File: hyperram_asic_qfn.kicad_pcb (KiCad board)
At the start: 4 copper layers, 59.5 x 60 mm, 45 parts, among them IC1 W25Q32JVSSIQ_TR, IC2 S27KL0641DABHI020, IC3 LP5907UVX-1.8_NOPB, IC4 LP5907UVX-3.3_NOPB, IC5 LP5907MFX-3.3_NOPB, IC6 MCP1824T-1802E_OT, J1 USB_B_Micro, J2 Conn_02x03_Counter_Clockwise, J3 1156915, J4 1156915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

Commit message: First try on component placement and routing.
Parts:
- added C19: 100n, Capacitor_SMD:C_0402_1005Metric_Pad0.74x0.62mm_HandSolder, F.Cu at (115.3, 70.6)
- added C20: 100n, Capacitor_SMD:C_0402_1005Metric_Pad0.74x0.62mm_HandSolder, F.Cu at (115.3, 72.6)
- added C21: 100n, Capacitor_SMD:C_0402_1005Metric_Pad0.74x0.62mm_HandSolder, F.Cu at (115.3, 74.5)
- added C22: 22u 25v, Capacitor_SMD:C_0805_2012Metric_Pad1.18x1.45mm_HandSolder, F.Cu at (111.3, 71.1)
- added C23: 1u 16v, Capacitor_SMD:C_0805_2012Metric_Pad1.18x1.45mm_HandSolder, F.Cu at (111.3, 74.1)
- added C24: 22u 25v, Capacitor_SMD:C_0805_2012Metric_Pad1.18x1.45mm_HandSolder, F.Cu at (111.3, 77.1)
- added J7: Conn_02x10_Odd_Even, Connector_PinHeader_2.54mm:PinHeader_2x10_P2.54mm_Vertical, F.Cu at (171.3, 73.0)
- added R5: 0, Resistor_SMD:R_0603_1608Metric, F.Cu at (176.5, 90.3)
- added R6: NC, Resistor_SMD:R_0603_1608Metric, F.Cu at (176.6, 87.6)
- added TP7: TestPoint, TestPoint:TestPoint_Pad_D1.0mm, F.Cu at (175.7, 93.2)
- C10, C2, C4, C5, C6, C7, C8, C9: value 22n -> 100n
- C18: value 1u 16v -> 100n; footprint Capacitor_SMD:C_0805_2012Metric_Pad1.18x1.45mm_HandSolder -> Capacitor_SMD:C_0402_1005Metric_Pad0.74x0.62mm_HandSolder
- J2: value Conn_02x03_Counter_Clockwise -> Conn_02x06_Odd_Even; footprint Connector_PinHeader_2.54mm:PinHeader_2x03_P2.54mm_Vertical -> Connector_PinHeader_2.54mm:PinHeader_2x06_P2.54mm_Vertical
- R4: value 220 -> 2k2
- U1: value CARAVEL -> CARAVEL_QFN; footprint hyperram_asic_qfn:WLCSP-60_P0.5mm -> Package_DFN_QFN:QFN-64-1EP_9x9mm_P0.5mm_EP7.65x7.65mm
- moved D2 71.1 mm to (101.6, 71.9)
- moved R2 71.1 mm to (101.6, 77.2)
- moved J2 54.7 mm to (126.0, 92.3), turned to 0 degrees
- moved C1 53.6 mm to (112.8, 96.9)
- moved IC1 53.6 mm to (117.4, 99.9)
- moved R3 39.4 mm to (147.2, 105.7)
- moved J4 39.4 mm to (148.5, 114.8), turned to 180 degrees
- moved RN3 28.2 mm to (182.0, 105.8)
- moved RN1 27.8 mm to (153.6, 105.7)
- moved J3 24.7 mm to (179.5, 114.8), turned to 180 degrees
- moved TP2 20.1 mm to (136.8, 85.5), turned to -90 degrees
- moved TP5 17.6 mm to (143.4, 85.5), turned to -90 degrees
- moved Y1 17.2 mm to (135.7, 79.3), turned to -90 degrees
- moved C6 17.0 mm to (144.1, 91.0)
- moved C10 16.7 mm to (144.4, 95.1)
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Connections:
- C10 pad 1: +1V8 -> VCC
- C17 pad 1: +1V8 -> VCC
- C6 pad 1: +1V8 -> VCC
- C8 pad 1: +1V8 -> VCC
- J2 pad 1: /mgmt_spi_cs -> +3V3
- J2 pad 2: /mgmt_spi_di -> +3V3
- J2 pad 3: /mgmt_spi_clk -> GND
- J2 pad 6: +5V -> /mgmt_spi_di
- RN1 pad 1: /cvl_hr_csn -> /cvl_hr_rwds
- RN1 pad 2: /cvl_hr_clk -> /cvl_hr_clkn
- RN1 pad 3: /cvl_hr_clkn -> /cvl_hr_clk
- RN1 pad 4: /cvl_hr_rwds -> /cvl_hr_csn
- RN1 pad 5: /hr_rwds -> /hr_csn
- RN1 pad 6: /hr_clkn -> /hr_clk
- RN1 pad 7: /hr_clk -> /hr_clkn
- RN1 pad 8: /hr_csn -> /hr_rwds
- RN2 pad 1: /cvl_hr_dq0 -> /cvl_hr_dq3
- RN2 pad 2: /cvl_hr_dq1 -> /cvl_hr_dq2
- RN2 pad 3: /cvl_hr_dq2 -> /cvl_hr_dq1
- RN2 pad 4: /cvl_hr_dq3 -> /cvl_hr_dq0
- RN2 pad 5: /hr_dq3 -> /hr_dq0
- RN2 pad 6: /hr_dq2 -> /hr_dq1
- RN2 pad 7: /hr_dq1 -> /hr_dq2
- RN2 pad 8: /hr_dq0 -> /hr_dq3
- RN3 pad 1: /cvl_hr_dq4 -> /cvl_hr_dq7
- RN3 pad 2: /cvl_hr_dq5 -> /cvl_hr_dq6
- RN3 pad 3: /cvl_hr_dq6 -> /cvl_hr_dq5
- RN3 pad 4: /cvl_hr_dq7 -> /cvl_hr_dq4
- RN3 pad 5: /hr_dq7 -> /hr_dq4
- RN3 pad 6: /hr_dq6 -> /hr_dq5
- RN3 pad 7: /hr_dq5 -> /hr_dq6
- RN3 pad 8: /hr_dq4 -> /hr_dq7
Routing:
- net GND: track 132.3 -> 40.9 mm, vias 80 -> 35
- net /hr_rstn: track 35.9 -> 5.40 mm
- net /mgmt_spi_do: track 30.4 -> 0.00 mm
- net +3V3: track 55.4 -> 26.1 mm, vias 14 -> 9
- net /hr_dq2: track 26.8 -> 0.00 mm, vias 2 -> 0
- net /hr_csn: track 33.7 -> 7.68 mm
- net /hr_dq3: track 28.6 -> 3.61 mm
- net /cvl_hr_rstn: track 22.7 -> 0.00 mm
- net /hr_dq1: track 22.7 -> 0.00 mm
- net /hr_clk: track 31.0 -> 10.1 mm
- net /flash_clk: track 20.1 -> 0.00 mm
- net +1V8: track 24.2 -> 4.55 mm, vias 7 -> 0
- net /mgmt_spi_di: track 19.4 -> 0.00 mm
- net /cvl_hr_csn: track 19.0 -> 0.00 mm
- net /mgmt_spi_clk: track 18.7 -> 0.00 mm
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- removed copper zone on B.Cu, net +1V8
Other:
- board size 59.5 x 60 mm -> 79.5 x 70 mm

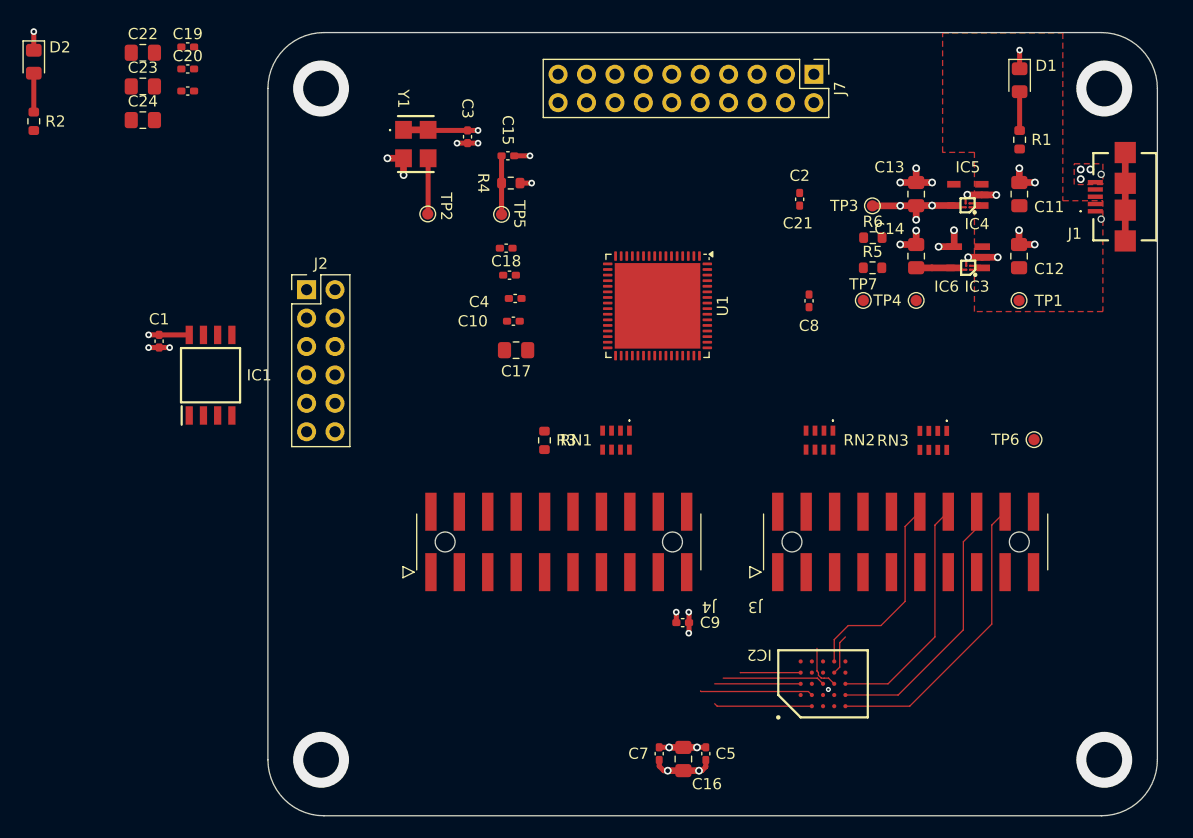
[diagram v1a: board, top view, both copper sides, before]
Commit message: Adjusted placement of some components and started routing tracks between ASIC and HyperRAM chip.
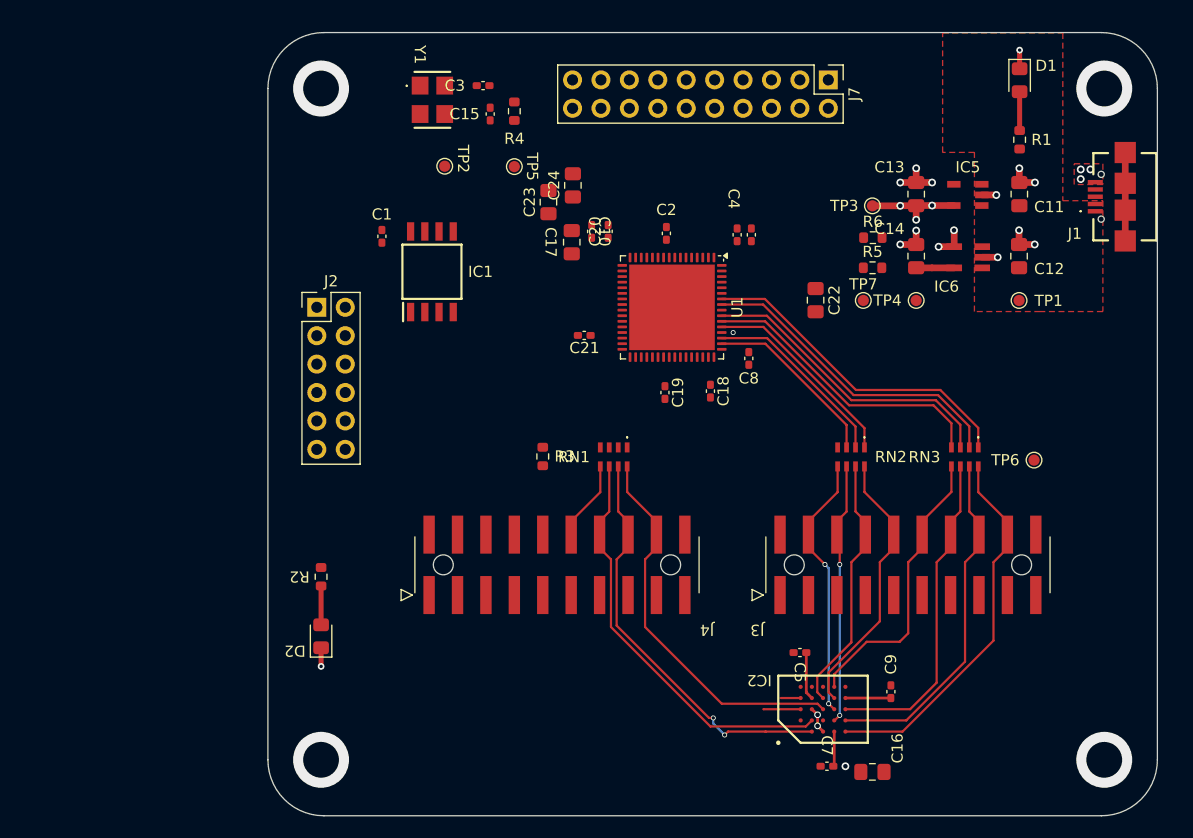
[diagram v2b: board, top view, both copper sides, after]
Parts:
- removed IC3: LP5907UVX-1.8_NOPB, hyperram_asic_qfn:BGA4C35P2X2_64X64X44
- removed IC4: LP5907UVX-3.3_NOPB, hyperram_asic_qfn:BGA4C35P2X2_64X64X33
- moved C22 64.1 mm to (171.4, 93.2), turned to -90 degrees
- moved D2 57.4 mm to (127.3, 123.3), turned to 90 degrees
- moved C19 52.7 mm to (158.0, 101.5), turned to -90 degrees
- moved R2 48.1 mm to (127.3, 117.9), turned to -90 degrees
- moved C21 41.6 mm to (150.8, 96.4), turned to 180 degrees
- moved C20 40.3 mm to (152.9, 87.1), turned to 90 degrees
- moved C24 38.9 mm to (149.8, 83.0), turned to 90 degrees
- moved C23 37.7 mm to (147.6, 84.5), turned to 90 degrees
- moved C18 22.3 mm to (162.1, 101.3), turned to -90 degrees
- moved C1 22.0 mm to (132.7, 87.5)
- moved C6 21.9 mm to (165.7, 87.4), turned to 90 degrees
- moved IC1 21.8 mm to (137.2, 90.7)
- moved C4 20.6 mm to (164.4, 87.4), turned to 90 degrees
- moved C9 19.6 mm to (178.2, 128.2), turned to 90 degrees
- moved C16 16.9 mm to (176.5, 135.4), turned to 0 degrees
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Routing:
- net /cvl_hr_dq7: track 0.00 -> 29.4 mm
- net /cvl_hr_dq6: track 0.00 -> 28.5 mm
- net /hr_clkn: track 8.78 -> 36.9 mm, vias 0 -> 2
- net /cvl_hr_dq5: track 0.00 -> 27.4 mm
- net /hr_clk: track 10.1 -> 37.0 mm
- net /cvl_hr_dq4: track 0.00 -> 26.5 mm
- net /hr_rwds: track 9.13 -> 34.8 mm
- net /hr_dq1: track 0.00 -> 23.4 mm, vias 0 -> 2
- net /hr_dq2: track 0.00 -> 23.1 mm
- net /hr_dq3: track 3.61 -> 24.4 mm
- net /hr_dq0: track 4.19 -> 23.7 mm, vias 0 -> 2
- net /cvl_hr_dq3: track 0.00 -> 18.2 mm
- net GND: track 40.9 -> 23.4 mm, vias 35 -> 25
- net /cvl_hr_dq2: track 0.00 -> 17.1 mm
- net /cvl_hr_dq1: track 0.00 -> 16.2 mm
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
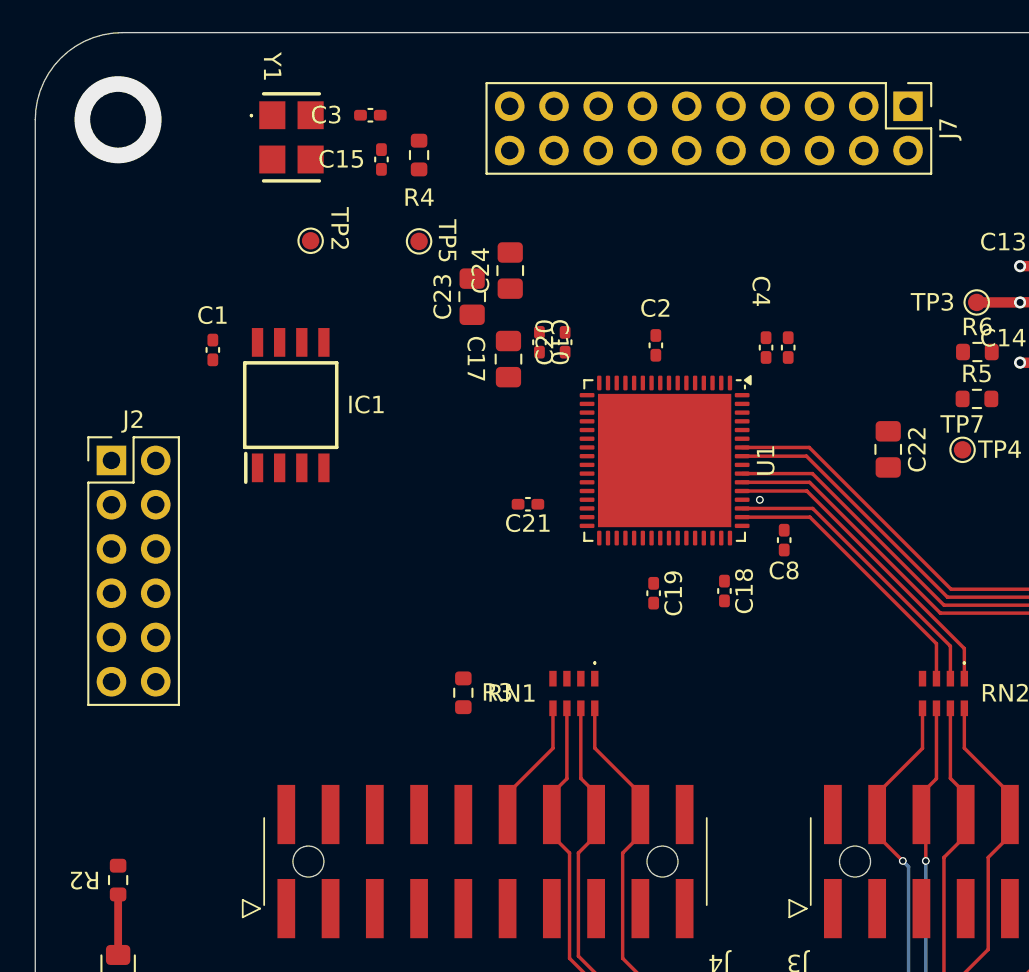
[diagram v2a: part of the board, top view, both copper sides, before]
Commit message: First try for routing digital signals (DSPI, GPIOs, CLK, RST)
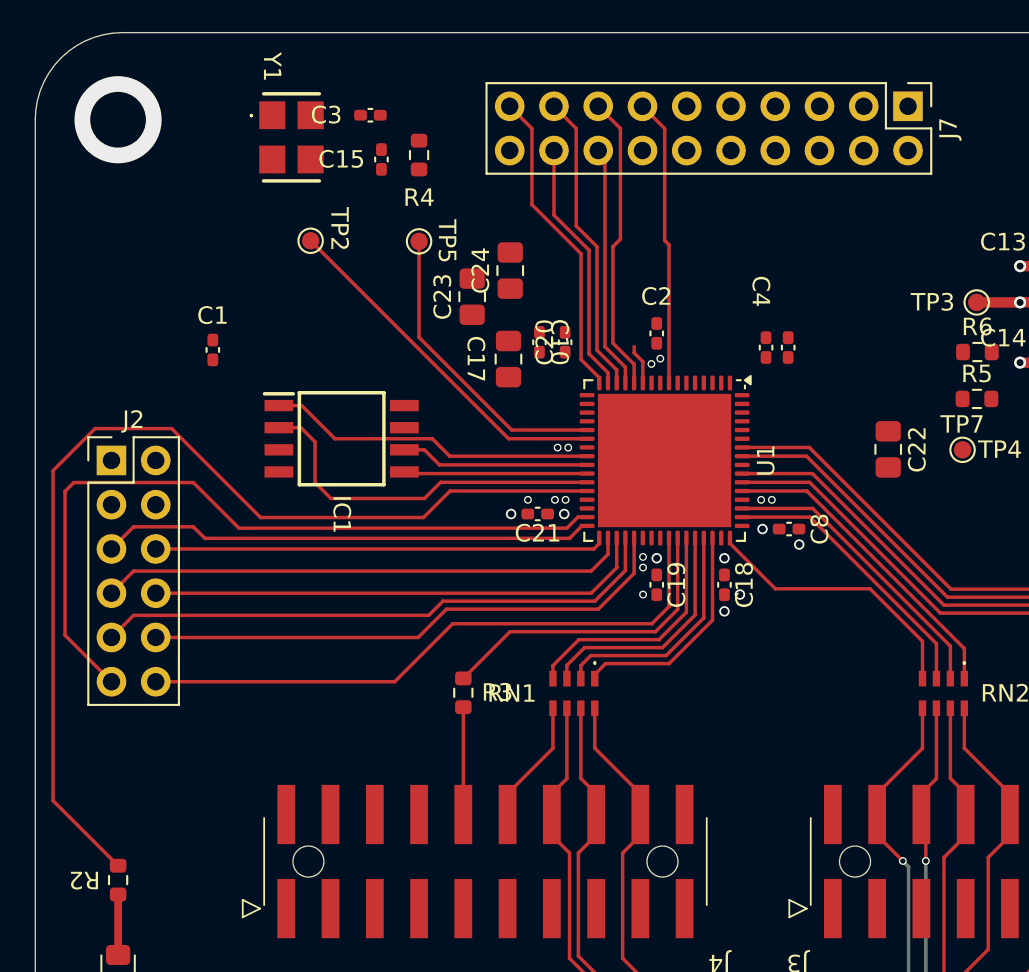
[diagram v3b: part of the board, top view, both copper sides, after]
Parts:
- moved IC1 3.50 mm to (140.1, 92.6), turned to 0 degrees
- moved C21 0.79 mm to (151.3, 96.9)
- moved C8 0.69 mm to (165.8, 97.8), turned to 0 degrees
- moved C2 0.69 mm to (158.2, 86.6)
- moved C19 0.51 mm to (158.2, 101.0)
- moved C18 0.36 mm to (162.1, 101.0)
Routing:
- net /gpio: track 0.00 -> 58.6 mm
- net /gpio0: track 0.00 -> 43.5 mm
- net /gpio7: track 0.00 -> 35.2 mm
- net /uart_rx: track 0.00 -> 32.9 mm
- net /uart_tx: track 0.00 -> 31.0 mm
- net /mgmt_spi_cs: track 0.00 -> 30.4 mm
- net /mgmt_spi_clk: track 0.00 -> 28.8 mm
- net /mgmt_spi_do: track 0.00 -> 28.4 mm
- net /mgmt_spi_di: track 0.00 -> 25.9 mm
- net /flash_io1: track 0.00 -> 21.1 mm
- net /clock: track 0.00 -> 20.6 mm
- net /flash_csb: track 0.00 -> 18.9 mm
- net /cvl_hr_rstn: track 0.00 -> 18.0 mm
- net /gpio37: track 0.00 -> 18.0 mm
- net /gpio35: track 0.00 -> 17.4 mm
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
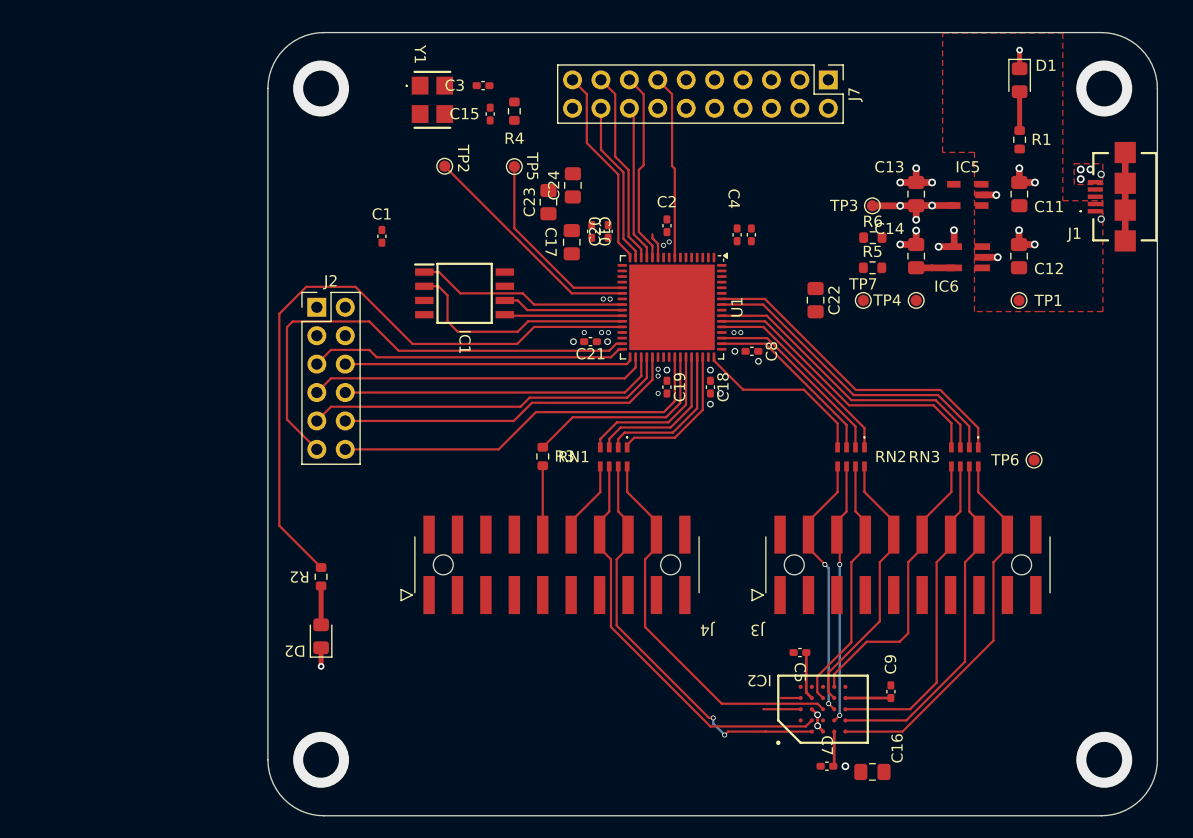
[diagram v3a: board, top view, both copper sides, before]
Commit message: Improved placement. Routed all digital signals.
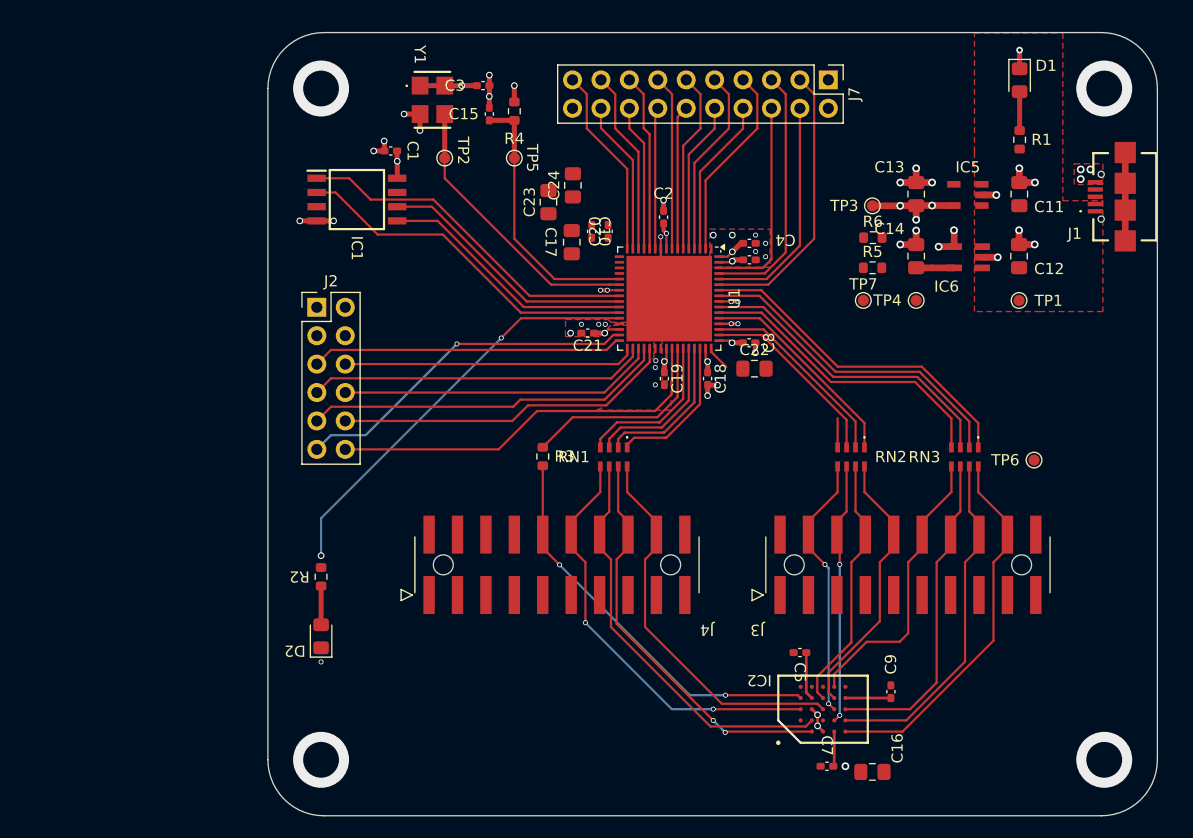
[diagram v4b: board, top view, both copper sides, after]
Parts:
- moved IC1 12.8 mm to (130.5, 84.2)
- moved C22 8.20 mm to (166.0, 99.3), turned to 0 degrees
- moved C1 7.67 mm to (133.5, 79.9), turned to 180 degrees
- moved C6 2.24 mm to (165.5, 89.6), turned to 0 degrees
- moved C4 1.33 mm to (165.5, 88.1), turned to 0 degrees
- moved C2 0.82 mm to (157.9, 85.8)
- moved U1 0.82 mm to (158.4, 93.1)
- moved C21 0.80 mm to (151.1, 96.2)
- moved C18 0.80 mm to (161.8, 100.2)
- moved C8 0.80 mm to (165.5, 97.0)
- moved C19 0.80 mm to (157.9, 100.2)
- moved TP5 0.76 mm to (144.5, 80.5)
- moved TP2 0.73 mm to (138.3, 80.5)
- moved C15 0.08 mm to (142.3, 76.6)
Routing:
- net /hr_rstn: track 7.93 -> 36.0 mm, vias 0 -> 2
- net /hr_csn: track 10.5 -> 38.0 mm, vias 0 -> 2
- net /gpio21: track 0.00 -> 24.9 mm
- net GND: track 23.4 -> 47.1 mm, vias 39 -> 56
- net /gpio23: track 0.00 -> 22.7 mm
- net /gpio: track 58.6 -> 37.4 mm, vias 0 -> 2
- net +3V3: track 20.0 -> 40.8 mm, vias 7 -> 11
- net /gpio22: track 0.00 -> 20.7 mm
- net /gpio24: track 0.00 -> 18.5 mm
- net /gpio25: track 0.00 -> 17.5 mm
- net /gpio27: track 0.00 -> 16.9 mm
- net /gpio29: track 0.00 -> 16.3 mm
- net /gpio26: track 0.00 -> 14.2 mm
- net /gpio28: track 0.00 -> 13.5 mm
- net /gpio30: track 0.00 -> 12.9 mm
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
